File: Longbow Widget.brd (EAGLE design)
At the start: 35 x 18 mm, 32 parts, among them J0 CONN_6SCREW_2.54, J1 CONN_6SCREW_2.54, J2 87832-14MALE, Q2 DMG3404, Q6 FDN360P, U1 TPS7A0533DBV

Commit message: Updated Longbow Widget to use new Frames
Updated to used new frames without Creative Commons text (caused issues)
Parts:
- removed FRAME1: (no value), bschulz:CREATIVE_COMMONS
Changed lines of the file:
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@@
 <attribute name="VALUE_PART" value="10" x="25.4" y="22.606" size="1.778" layer="27" display="off"/>
-</element>
-<element name="FRAME1" library="bschulz" package="CREATIVE_COMMONS" value="" x="-29.89530625" y="0">
-<attribute name="DESIGNER" value="Bobby Schulz" x="-29.89530625" y="0" size="1.778" layer="27" display="off"/>
-<attribute name="PROJECT" value="Longbow" x="-29.89530625" y="0" size="1.778" layer="27" display="off"/>
-<attribute name="REV" value="v0.1" x="-29.89530625" y="0" size="1.778" layer="27" display="off"/>
 </element>
 </elements>
@@
 <wire x1="15.067" y1="23.287" x2="15.067" y2="23.605" width="0.1524" layer="1"/>
 <wire x1="15.382" y1="22.972" x2="15.067" y2="23.287" width="0.1524" layer="1"/>
+<wire x1="28.829" y1="21.4686375" x2="28.829" y2="21.59" width="0" layer="19" extent="16-16"/>
+<wire x1="36.195" y1="11.745821875" x2="29.21" y2="15.24" width="0" layer="19" extent="16-16"/>
 </signal>
 <signal name="SCL">

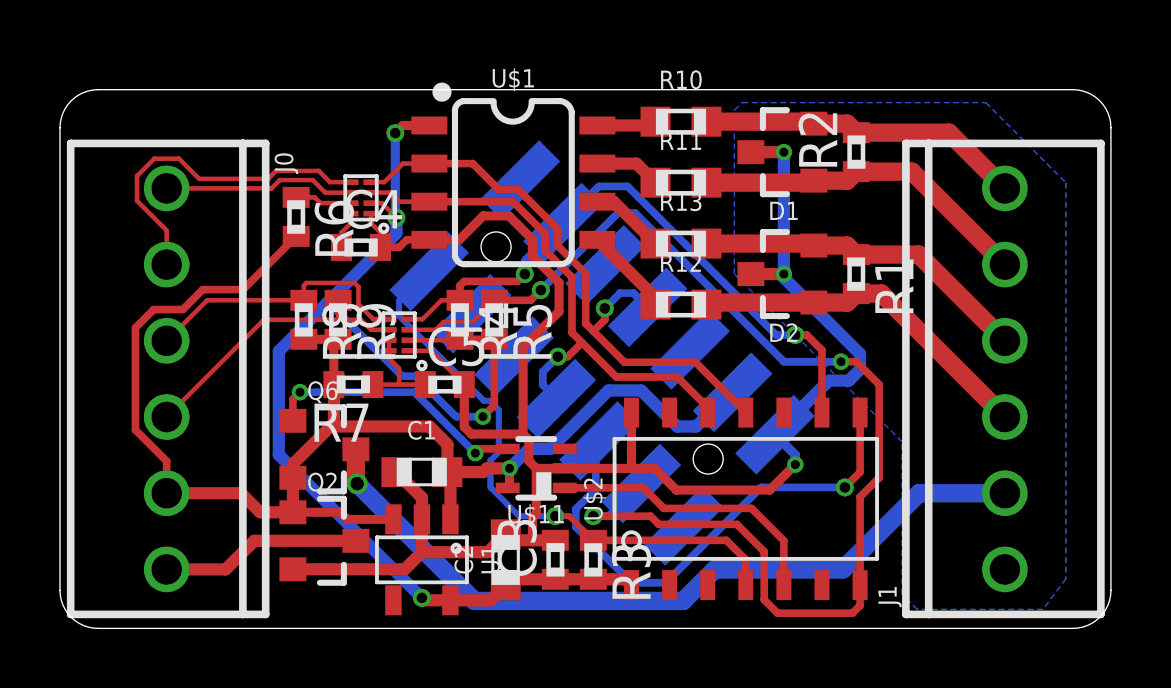
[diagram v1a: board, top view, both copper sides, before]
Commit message: Updated Longbow Widget, v0.2 ready for review
Made changes to new level shifters, RS485 driver with output shutoff, replaced mosfet with load switch, converted MCU to QFN package. Ready for final review
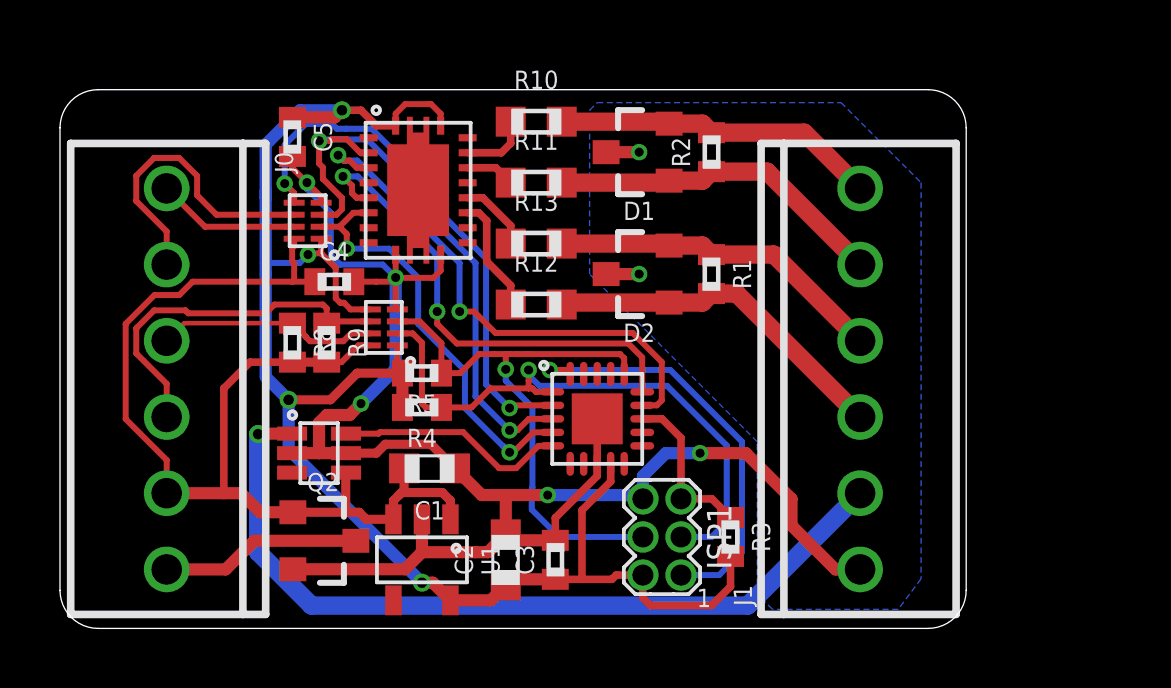
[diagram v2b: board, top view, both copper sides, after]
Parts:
- removed J2: 87832-14MALE, bschulz:87832-14
- removed Q6: FDN360P, bschulz:SOT23-3
- removed R6, R7: 200k, bschulz_passives:R0402
- removed U$11: MIC842H, bschulz:DCK_R-PDSO-G5
- added ISP1: AVRISP1.27MM, bschulz:2X3_1.27
- added U2: SN65HVD33RHL, bschulz:VQFN-20_POWER
- U$1: value SN65HVD30 -> MIC94090C6; device bschulz:SO08 -> bschulz:SC-70_6
- U$2: value ATTINY441/841841 -> ATTINY441/841VQFN; device bschulz:SOIC_14 -> bschulz:VQFN-20
- U$3, U$6: value LSF0102DQE -> TXS0102DQM; device bschulz:DQE_R-PX2SON-N8 -> bschulz:DQM_R-PX2SON-N8
- moved U$1 11.1 mm to (13.3, 15.6)
- moved C5 9.69 mm to (12.4, 26.2), turned to 270 degrees
- moved U$2 5.63 mm to (22.6, 16.8)
- moved D1 4.83 mm to (24.0, 25.7)
- moved D2 4.83 mm to (24.0, 21.6)
- moved J1 4.83 mm to (31.4, 18.1)
- moved R1 4.83 mm to (26.4, 21.6)
- moved R2 4.83 mm to (26.4, 25.7)
- moved R10 4.83 mm to (20.6, 26.7)
- moved R11 4.83 mm to (20.6, 24.6)
- moved R12 4.83 mm to (20.6, 20.6)
- moved R13 4.83 mm to (20.6, 22.6)
- moved R3 4.64 mm to (27.1, 12.8)
- moved R4 3.19 mm to (16.8, 17.1), turned to 180 degrees
- moved R5 3.00 mm to (16.8, 18.3), turned to 180 degrees
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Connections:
- removed net N$1: C5.1, R7.1, U$3.7, U$3.8
- removed net N$3: C4.1, R6.1, U$6.7, U$6.8
- removed net N$4: Q6.1, U$11.4
- new net !RE: U$2.14, U2.4
- new net DE: U$2.15, U2.6
- new net UART_EN: U$2.2, U$6.5
- net /RESET: now also ISP1.5, U$2.13; no longer J2.13, U$2.4
- net 3V3: now also C5.1, ISP1.2, U$2.9, U$3.1, U$3.5, U$6.1, U2.1, U2.20; no longer U$1.1, U$2.1, U$3.2, U$6.2
- net 3V3_CTRL: now also U$1.6; no longer U$11.1
- net GND: now also ISP1.6, U$1.2, U$1.5, U$2.8, U$2.EP, U$3.4, U$6.4, U2.10, U2.11; no longer J2.2, U$1.4, U$11.2, U$2.14, U$3.1, U$6.1
- net MISO: now also ISP1.1, U$2.20; no longer J2.5, U$2.8
- net N$2: now also U2.18; no longer U$1.8
- net N$5: now also U2.17; no longer U$1.7
- net N$6: now also U2.14; no longer U$1.5
- net N$7: now also U2.15; no longer U$1.6
- net RX: now also U$2.4, U$6.2, U2.7; no longer J2.7, U$1.3, U$2.12, U$6.3
- net RX_HV: now also U$6.7; no longer U$6.6
- net SCL: now also ISP1.3, U$2.1, U$3.2; no longer J2.12, U$2.9, U$3.4
- net SCL_HV: now also U$3.7; no longer U$3.5
- net SDA: now also ISP1.4, U$2.16; no longer J2.3, U$2.7
- net TX: now also U$2.3, U$6.3, U2.3; no longer J2.8, U$1.2, U$2.11, U$6.4
- net TX_HV: now also U$6.6; no longer U$6.5
- net VIN+: now also C4.1, U$1.4, U$3.8, U$6.8; no longer J2.4, Q6.2, R6.2, R7.2, U$11.5
- net VOUT: now also U$1.1; no longer Q6.3
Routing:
- net SDA: track 40.6 -> 19.3 mm, vias 3 -> 1
- net UART_EN: track 0.00 -> 18.0 mm, vias 0 -> 2
- net !RE: track 0.00 -> 17.8 mm, vias 0 -> 2
- net DE: track 0.00 -> 16.3 mm, vias 0 -> 2
- net 3V3: track 41.1 -> 55.4 mm
- net /RESET: track 19.6 -> 5.50 mm, vias 1 -> 0
- net VIN+: track 47.3 -> 37.2 mm, vias 1 -> 0
- net N$4: track 8.88 -> 0.00 mm, vias 2 -> 0
- net RX: track 18.6 -> 14.2 mm, vias 1 -> 2
- net N$3: track 3.51 -> 0.00 mm
- net N$1: track 3.36 -> 0.00 mm
- net MISO: track 16.9 -> 14.2 mm
- net SDA_HV: track 9.54 -> 12.2 mm
- net SCL_HV: track 9.34 -> 7.40 mm
- net 3V3_CTRL: track 9.51 -> 7.70 mm
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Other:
- board size 35 x 18 mm -> 30.2 x 18 mm
- board text added: "Longbow Widget v0.2 -------------- Designed by Northern Widget and University of Minnesota"
- board text removed: "Northern Widget Bobby Schulz"

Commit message: Longbow Widget v0.2 sent to fab
Minor edits to silkscreen on longbow widget, v0.2 timeline, generated gerbers for Longbow Widget
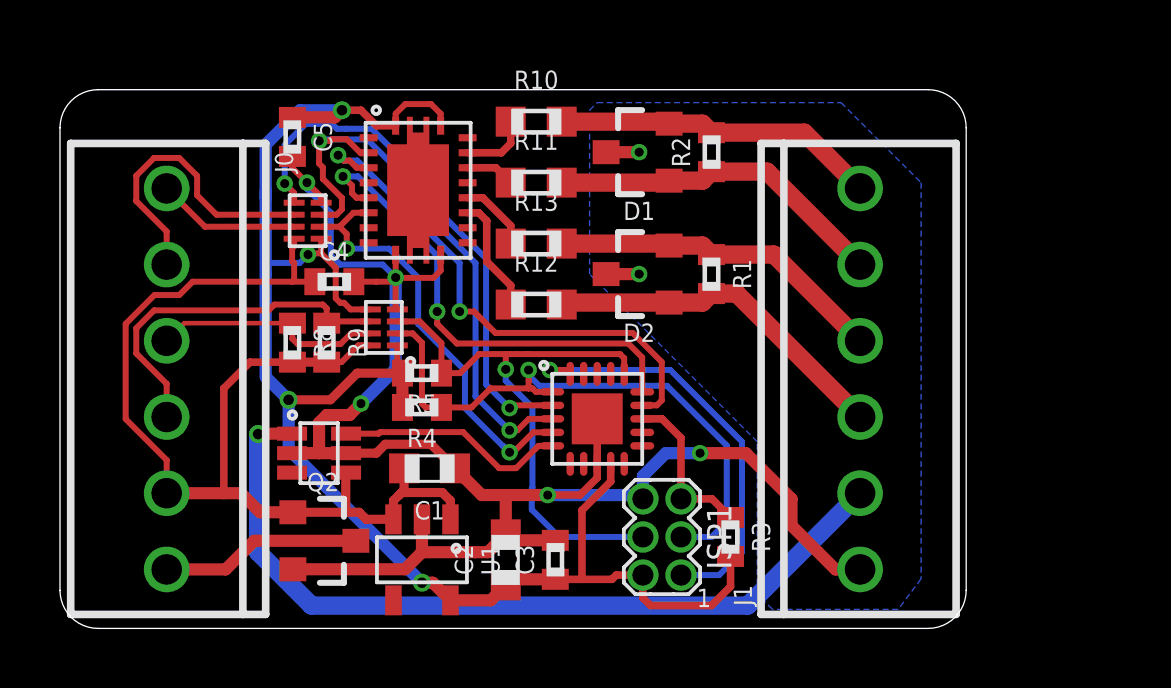
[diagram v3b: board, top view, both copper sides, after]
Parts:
- added U$4: NWLOGO_MED, awickert:NWLOGO_MED
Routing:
- net GND: track 62.1 -> 61.4 mm
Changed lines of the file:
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@@
 <grid distance="50" unitdist="mil" unit="mm" style="lines" multiple="1" display="no" altdistance="5" altunitdist="mil" altunit="mm"/>
 <layers>
-<layer number="1" name="Top" color="4" fill="1" visible="yes" active="yes"/>
+<layer number="1" name="Top" color="4" fill="1" visible="no" active="yes"/>
 <layer number="2" name="Route2" color="1" fill="3" visible="no" active="no"/>
 <layer number="3" name="Route3" color="4" fill="3" visible="no" active="no"/>
@@
 <layer number="17" name="Pads" color="2" fill="1" visible="yes" active="yes"/>
 <layer number="18" name="Vias" color="2" fill="1" visible="yes" active="yes"/>
-<layer number="19" name="Unrouted" color="6" fill="1" visible="yes" active="yes"/>
+<layer number="19" name="Unrouted" color="6" fill="1" visible="no" active="yes"/>
 <layer number="20" name="Dimension" color="24" fill="1" visible="yes" active="yes"/>
-<layer number="21" name="tPlace" color="7" fill="1" visible="yes" active="yes"/>
+<layer number="21" name="tPlace" color="7" fill="1" visible="no" active="yes"/>
 <layer number="22" name="bPlace" color="7" fill="1" visible="yes" active="yes"/>
-<layer number="23" name="tOrigins" color="15" fill="1" visible="yes" active="yes"/>
+<layer number="23" name="tOrigins" color="15" fill="1" visible="no" active="yes"/>
 <layer number="24" name="bOrigins" color="15" fill="1" visible="yes" active="yes"/>
 <layer number="25" name="tNames" color="7" fill="1" visible="no" active="yes"/>
@@
 <layer number="30" name="bStop" color="7" fill="6" visible="no" active="yes"/>
 <layer number="31" name="tCream" color="7" fill="4" visible="no" active="yes"/>
-<layer number="32" name="bCream" color="7" fill="5" visible="no" active="yes"/>
+<layer number="32" name="bCream" color="7" fill="5" visible="yes" active="yes"/>
 <layer number="33" name="tFinish" color="6" fill="3" visible="no" active="yes"/>
 <layer number="34" name="bFinish" color="6" fill="6" visible="no" active="yes"/>
@@
 <layer number="37" name="tTest" color="7" fill="1" visible="no" active="yes"/>
 <layer number="38" name="bTest" color="7" fill="1" visible="no" active="yes"/>
-<layer number="39" name="tKeepout" color="4" fill="11" visible="yes" active="yes"/>
-<layer number="40" name="bKeepout" color="1" fill="11" visible="yes" active="yes"/>
-<layer number="41" name="tRestrict" color="4" fill="10" visible="yes" active="yes"/>
-<layer number="42" name="bRestrict" color="1" fill="10" visible="yes" active="yes"/>
+<layer number="39" name="tKeepout" color="4" fill="11" visible="no" active="yes"/>
+<layer number="40" name="bKeepout" color="1" fill="11" visible="no" active="yes"/>
+<layer number="41" name="tRestrict" color="4" fill="10" visible="no" active="yes"/>
+<layer number="42" name="bRestrict" color="1" fill="10" visible="no" active="yes"/>
 <layer number="43" name="vRestrict" color="2" fill="10" visible="no" active="yes"/>
 <layer number="44" name="Drills" color="7" fill="1" visible="yes" active="yes"/>
@@
 <layer number="49" name="Reference" color="7" fill="1" visible="no" active="yes"/>
 <layer number="50" name="dxf" color="7" fill="1" visible="no" active="no"/>
-<layer number="51" name="tDocu" color="7" fill="1" visible="yes" active="yes"/>
+<layer number="51" name="tDocu" color="7" fill="1" visible="no" active="yes"/>
 <layer number="52" name="bDocu" color="7" fill="1" visible="yes" active="yes"/>
 <layer number="53" name="tGND_GNDA" color="7" fill="1" visible="no" active="no"/>
@@
 <layer number="118" name="Rect_Pads" color="7" fill="1" visible="no" active="yes"/>
 <layer number="121" name="_tsilk" color="7" fill="1" visible="no" active="yes"/>
-<layer number="122" name="_bsilk" color="7" fill="1" visible="yes" active="yes"/>
+<layer number="122" name="_bsilk" color="7" fill="1" visible="no" active="yes"/>
 <layer number="123" name="tTestmark" color="7" fill="1" visible="no" active="yes"/>
 <layer number="124" name="bTestmark" color="7" fill="1" visible="no" active="yes"/>
@@
 <attribute name="MPN" value="GCM155R71C104KA55D" x="12.446" y="26.162" size="1.778" layer="27" rot="R270" display="off"/>
 </element>
+<element name="U$4" library="awickert" package="NWLOGO_MED" value="NWLOGO_MED" x="15.24" y="15.24" rot="MR0"/>
 </elements>
 <signals>
@@
 <wire x1="19.558" y1="12.915" x2="19.758" y2="12.715" width="0.4064" layer="1"/>
 <wire x1="19.758" y1="12.715" x2="21.209" y2="12.715" width="0.4064" layer="1"/>
-<wire x1="22.606" y1="15.264" x2="22.606" y2="14.859" width="0.254" layer="1"/>
-<wire x1="22.606" y1="14.859" x2="21.844" y2="14.097" width="0.254" layer="1"/>
-<wire x1="21.844" y1="14.097" x2="21.209" y2="13.462" width="0.254" layer="1"/>
-<wire x1="21.209" y1="13.462" x2="21.209" y2="12.715" width="0.254" layer="1"/>
 <wire x1="22.606" y1="15.264" x2="22.606" y2="16.764" width="0.254" layer="1"/>
 <wire x1="17.868" y1="15.113" x2="18.757" y2="14.224" width="0.4064" layer="1"/>
@@
 <wire x1="12.9326" y1="24.638" x2="12.446" y2="25.1246" width="0.2" layer="1"/>
 <wire x1="12.446" y1="25.1246" x2="12.446" y2="25.512" width="0.2" layer="1"/>
+<wire x1="22.606" y1="15.264" x2="22.606" y2="14.7987375" width="0.254" layer="1"/>
+<wire x1="22.0312625" y1="14.224" x2="20.955" y2="14.224" width="0.254" layer="1"/>
+<wire x1="22.606" y1="14.7987375" x2="22.0312625" y2="14.224" width="0.254" layer="1"/>
 </signal>
 <signal name="SCL">
@@
 <wire x1="8.255" y1="16.825821875" x2="8.255" y2="17.9312375" width="0.2" layer="1"/>
 <wire x1="8.255" y1="17.9312375" x2="7.24059375" y2="18.94564375" width="0.2" layer="1"/>
-<wire x1="11.557" y1="20.28260625" x2="8.97929375" y2="20.28260625" width="0.2" layer="1"/>
-<wire x1="7.83481875" y1="20.38023125" x2="8.88166875" y2="20.38023125" width="0.2" layer="1"/>
-<wire x1="8.97929375" y1="20.28260625" x2="8.88166875" y2="20.38023125" width="0.2" layer="1"/>
+<wire x1="11.654625" y1="20.38023125" x2="7.83481875" y2="20.38023125" width="0.2" layer="1"/>
 <wire x1="7.24059375" y1="19.78600625" x2="7.83481875" y2="20.38023125" width="0.2" layer="1"/>
-<wire x1="11.557" y1="20.28260625" x2="11.84839375" y2="20.574" width="0.2" layer="1"/>
+<wire x1="11.654625" y1="20.38023125" x2="11.84839375" y2="20.574" width="0.2" layer="1"/>
 <wire x1="11.84839375" y1="20.574" x2="11.84839375" y2="20.574" width="0.2" layer="1"/>
 <wire x1="11.84839375" y1="20.574" x2="13.462" y2="20.574" width="0.2" layer="1"/>
@@
 <wire x1="8.843178125" y1="19.954" x2="8.255" y2="19.365821875" width="0.1524" layer="1"/>
 <contactref element="U$3" pad="7"/>
-<wire x1="12.8866" y1="19.49945" x2="13.03445" y2="19.3516" width="0.2" layer="1"/>
-<wire x1="13.03445" y1="19.3516" x2="14.14355" y2="19.3516" width="0.2" layer="1"/>
-<wire x1="12.8866" y1="19.5134" x2="12.8866" y2="19.49945" width="0.2" layer="1"/>
-<wire x1="14.40395" y1="19.612" x2="15.044" y2="19.612" width="0.2" layer="1"/>
-<wire x1="14.14355" y1="19.3516" x2="14.40395" y2="19.612" width="0.2" layer="1"/>
-<wire x1="12.446" y1="19.954" x2="12.8866" y2="19.5134" width="0.2" layer="1"/>
+<wire x1="15.044" y1="19.612" x2="14.40395" y2="19.612" width="0.2" layer="1"/>
+<wire x1="14.40395" y1="19.612" x2="14.04835" y2="19.2564" width="0.2" layer="1"/>
+<wire x1="12.6206" y1="19.2564" x2="12.446" y2="19.431" width="0.2" layer="1"/>
+<wire x1="12.446" y1="19.431" x2="12.446" y2="19.954" width="0.2" layer="1"/>
+<wire x1="14.04835" y1="19.2564" x2="12.6206" y2="19.2564" width="0.2" layer="1"/>
 </signal>
 <signal name="TX_HV">
